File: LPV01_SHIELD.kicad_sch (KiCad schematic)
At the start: 89 parts, among them J1 Screw_Terminal_01x02, J10 SPI_header, J11 Power_socket, J12 USB1035-GF-P-0-B-B, J2 Screw_Terminal_01x02, J3 Screw_Terminal_01x02, J4 Screw_Terminal_01x02, J5 Screw_Terminal_01x02, J6 Screw_Terminal_01x02, J7 Screw_Terminal_01x02, J8 Screw_Terminal_01x02, J9 GPIO_header, Q1 BC817, Q2 BC817, Q3 BC817, Q4 BC817, Q5 BC817, Q6 BC817, Q7 BC817, Q8 BC817, SW1 SW_SPST, SW2 SW_SPST, SW3 SW_SPST, SW4 SW_SPST, SW5 SW_SPST, SW6 SW_SPST, SW7 SW_SPST, SW8 SW_SPST, U1 TLP175A, U10 MP2491C, U11 LT1086-3.3, U12 USB2517I-JZX, U13 FT2232HQ, U2 TLP175A, U3 TLP175A, U4 TLP175A, U5 TLP175A, U6 TLP175A, U7 TLP175A, U8 TLP175A, U9 MIC2026-1xM

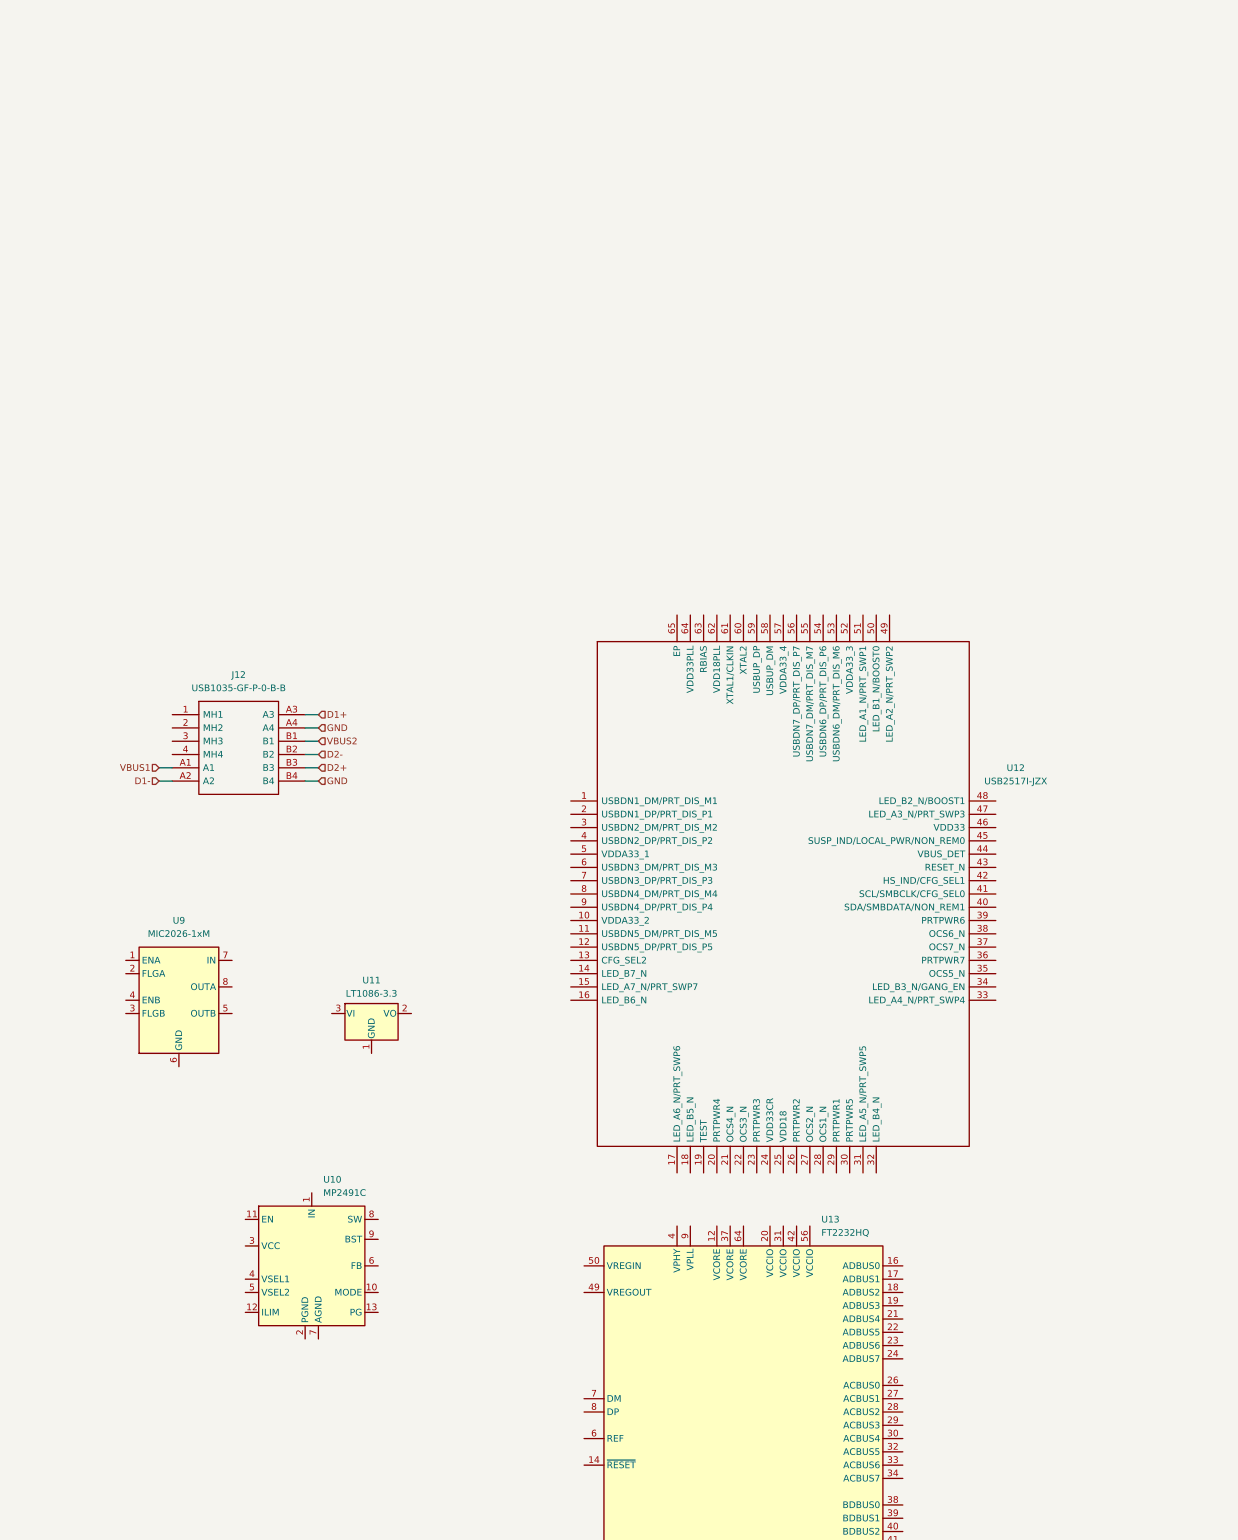
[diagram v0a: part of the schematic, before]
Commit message: Added some terminals and assigned footprints
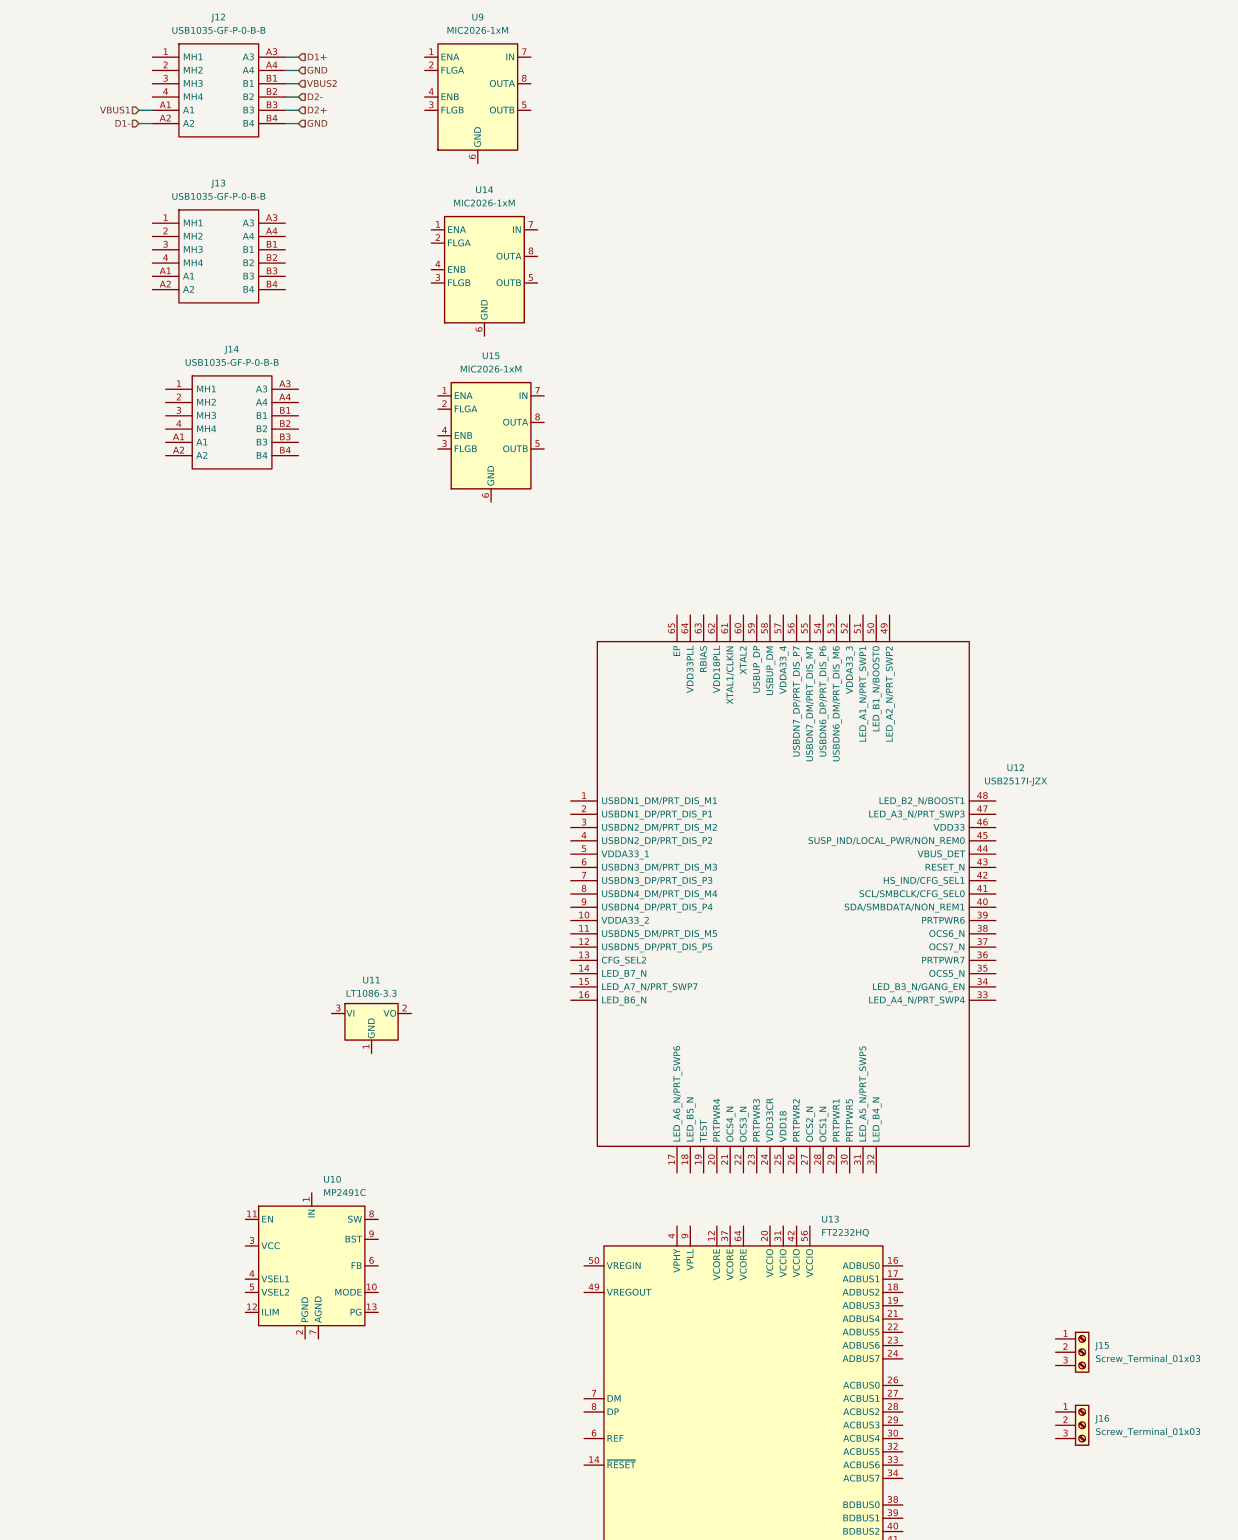
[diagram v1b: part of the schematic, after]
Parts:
- added J13, J14: USB1035-GF-P-0-B-B, SamacSys_Parts:USB1035GFP0BB, symbol SamacSys_Parts:USB1035-GF-P-0-B-B
- added J15, J16: Screw_Terminal_01x03, TerminalBlock_Phoenix:TerminalBlock_Phoenix_MKDS-1,5-3_1x03_P5.00mm_Horizontal, symbol Connector:Screw_Terminal_01x03
- added U14, U15: MIC2026-1xM, Package_SO:SOIC-8_3.9x4.9mm_P1.27mm, symbol Power_Management:MIC2026-1xM
- J12: footprint USB1035GFP0BB -> SamacSys_Parts:USB1035GFP0BB
- SW1, SW2, SW3, SW4, SW5, SW6, SW7, SW8: footprint (none) -> Button_Switch_SMD:SW_SPST_CK_RS282G05A3
- U11: footprint (none) -> Package_TO_SOT_SMD:TO-263-3_TabPin2
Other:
- moved on the sheet: J12, U9

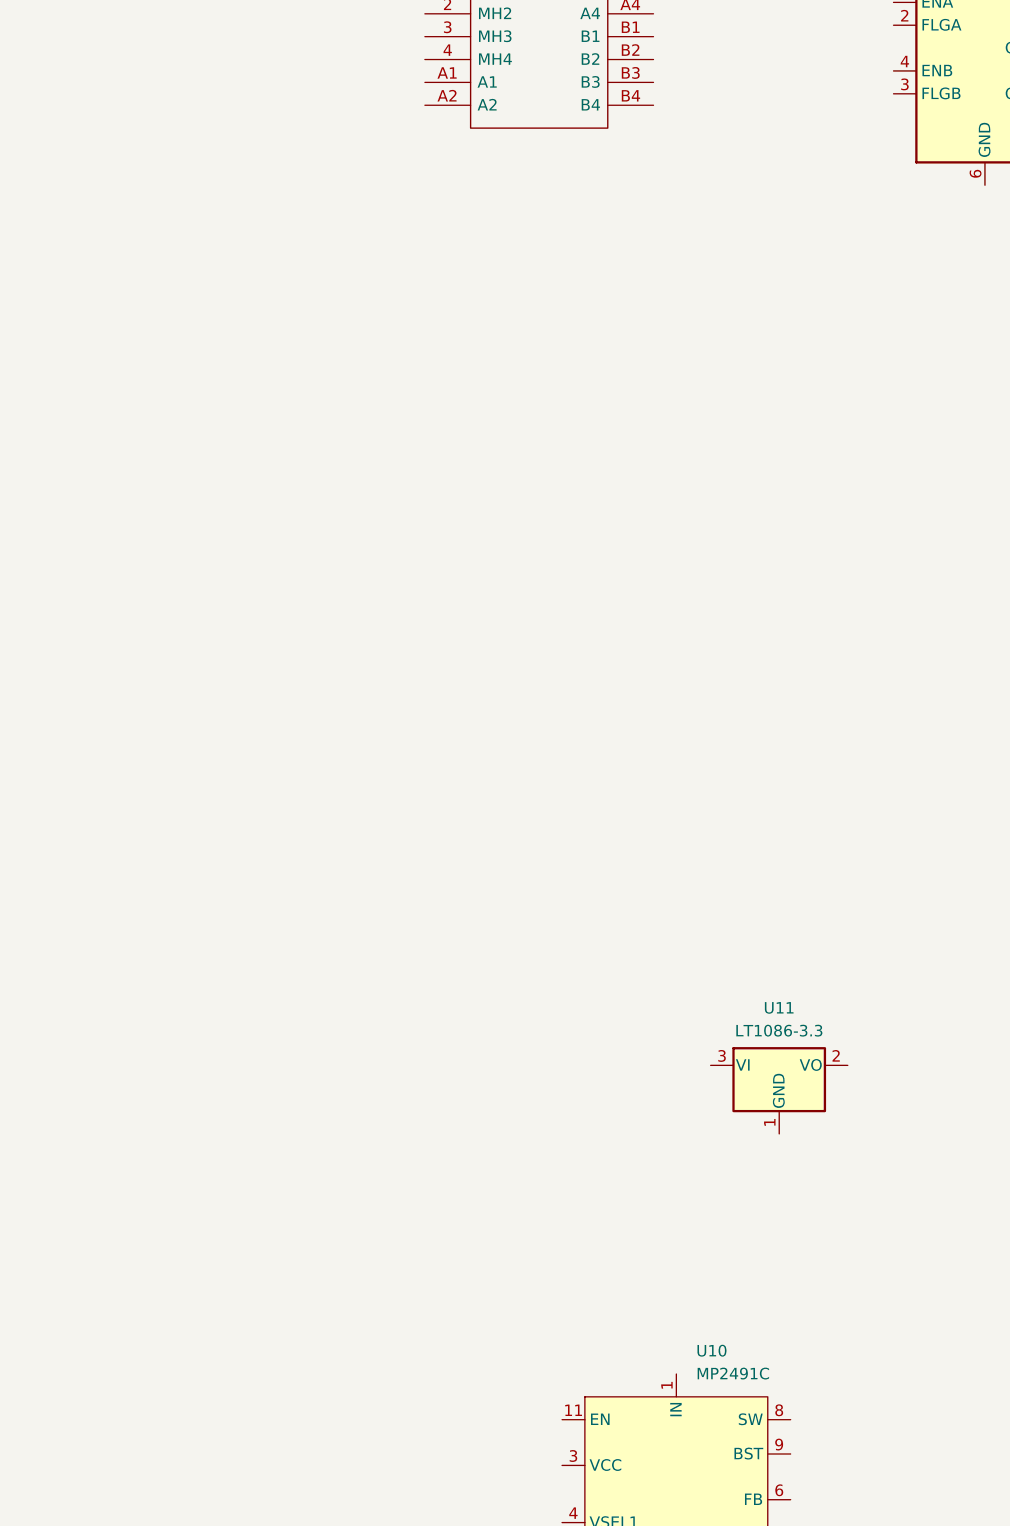
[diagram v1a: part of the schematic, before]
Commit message: Lengthening the board
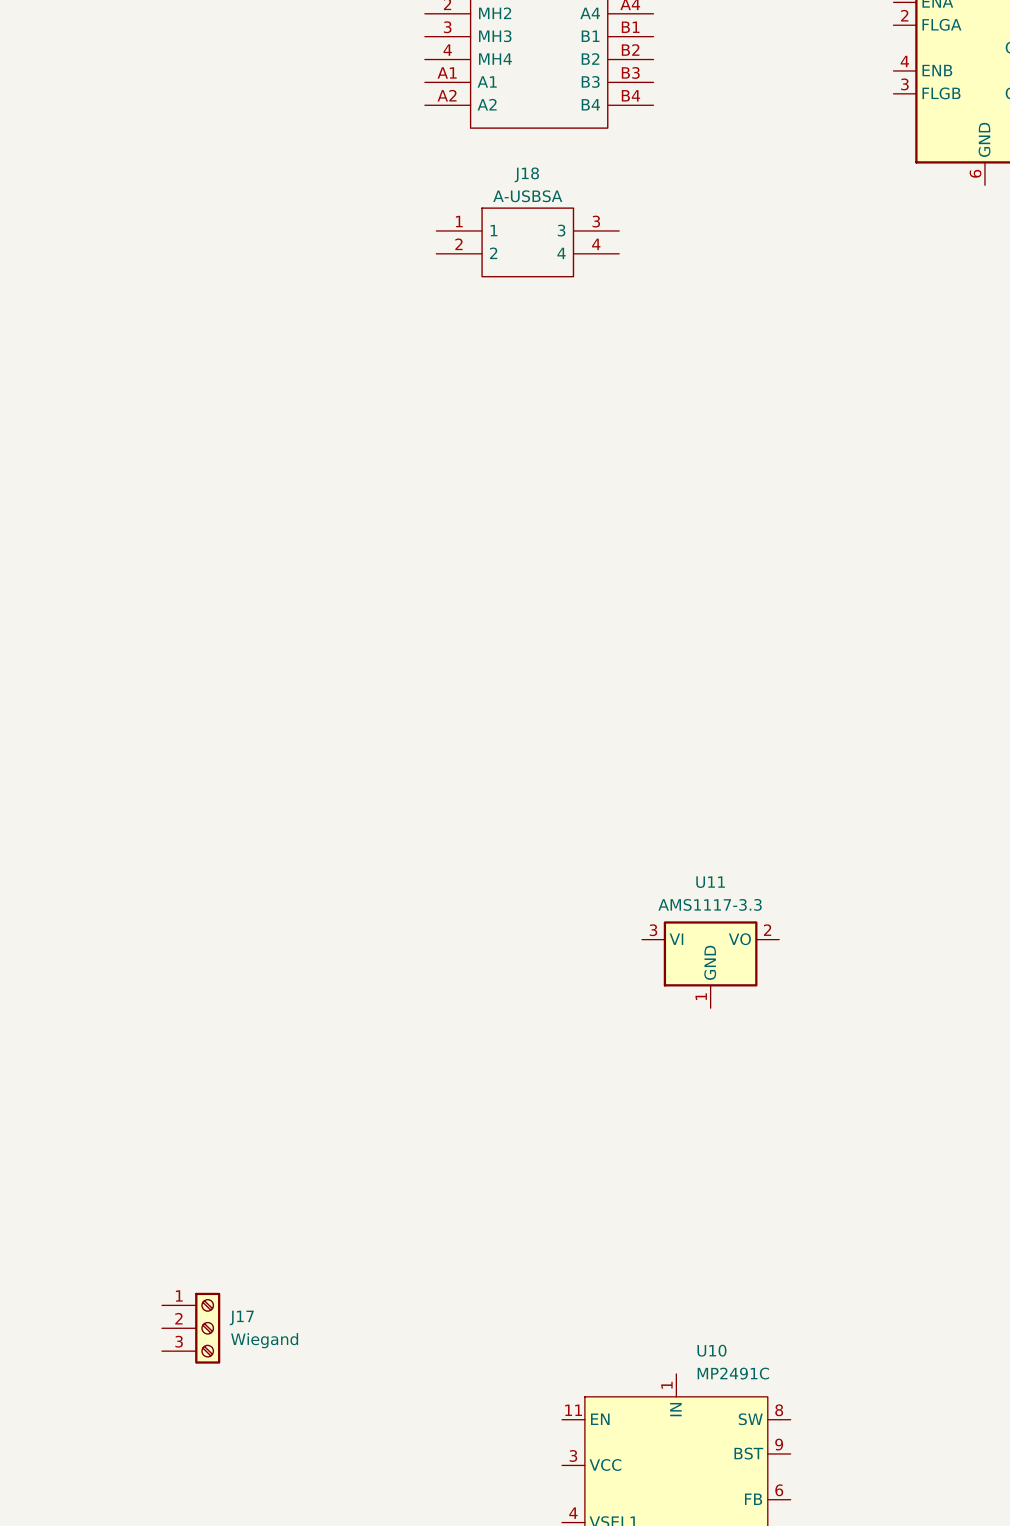
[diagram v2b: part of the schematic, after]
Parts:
- removed U11: LT1086-3.3, Package_TO_SOT_SMD:TO-263-3_TabPin2, symbol Regulator_Linear:LT1086-3.3
- added J17: Wiegand, TerminalBlock_Phoenix:TerminalBlock_Phoenix_MKDS-1,5-3_1x03_P5.00mm_Horizontal, symbol Connector:Screw_Terminal_01x03
- added J18: A-USBSA, A-USBSA, symbol SamacSys_Parts:A-USBSA
- added U11: AMS1117-3.3, Package_TO_SOT_SMD:SOT-223-3_TabPin2, symbol Regulator_Linear:AMS1117-3.3
- D10, D12, D14, D16, D2, D4, D6, D8: footprint Diode_SMD:D_SOD-123F -> Diode_SMD:D_SMA

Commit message: Length change
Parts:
- added C1: C, symbol Device:C
- added D17: D_Zener, symbol Device:D_Zener
- added J19, J20, J21, J22: Screw_Terminal_01x02, TerminalBlock_Phoenix:TerminalBlock_Phoenix_MKDS-1,5-2_1x02_P5.00mm_Horizontal, symbol Connector:Screw_Terminal_01x02
- added J23: GND, TerminalBlock_Phoenix:TerminalBlock_Phoenix_MKDS-1,5-3_1x03_P5.00mm_Horizontal, symbol Connector:Screw_Terminal_01x03
- added R33, R34: R, symbol Device:R

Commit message: Added power schematic
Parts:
- removed U10: MP2491C, HK:QFN-13_HK, symbol HK:MP2491C_HK
- removed U11: AMS1117-3.3, Package_TO_SOT_SMD:SOT-223-3_TabPin2, symbol Regulator_Linear:AMS1117-3.3
- removed U14, U15, U9: MIC2026-1xM, Package_SO:SOIC-8_3.9x4.9mm_P1.27mm, symbol Power_Management:MIC2026-1xM
- added U16: M24C02-FMN, Package_SO:SOIC-8_3.9x4.9mm_P1.27mm, symbol Memory_EEPROM:M24C02-FMN
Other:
- added sheet Power_distribution (Power_distribution.kicad_sch)

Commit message: Power schematic update of one DC/DC converter
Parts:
- removed C1: C, symbol Device:C
- removed D17: D_Zener, symbol Device:D_Zener
- removed R33, R34: R, symbol Device:R
